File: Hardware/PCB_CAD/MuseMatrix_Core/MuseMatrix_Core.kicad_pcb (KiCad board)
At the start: 2 copper layers, 65 parts, among them J10 Conn_01x03_Pin, J11 Conn_01x03_Pin, J12 Conn_01x03_Pin, J2 Conn_01x07_Socket, J3 Conn_01x03_Pin, J4 Conn_01x07_Socket, J5 Conn_01x07_Socket, J6 Conn_01x03_Pin, J7 Conn_01x03_Pin, J8 Conn_01x03_Pin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

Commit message: more pcb edit
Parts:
- added H1: MountingHole, MountingHole:MountingHole_2.1mm, F.Cu at (25.0, 17.5)
- added H2: MountingHole, MountingHole:MountingHole_2.1mm, F.Cu at (50.0, 17.5)
- added H3: MountingHole, MountingHole:MountingHole_2.1mm, F.Cu at (50.0, 173.5)
- added H4: MountingHole, MountingHole:MountingHole_2.1mm, F.Cu at (25.0, 173.5)
- added H5: MountingHole, MountingHole:MountingHole_2.1mm, F.Cu at (56.0, 17.5)
- added H6: MountingHole, MountingHole:MountingHole_2.1mm, F.Cu at (81.0, 17.5)
- added H7: MountingHole, MountingHole:MountingHole_2.1mm, F.Cu at (56.0, 128.0)
- added H8: MountingHole, MountingHole:MountingHole_2.1mm, F.Cu at (81.0, 128.0)
- added J1: Raspberry_Pi_4, Connector_PinHeader_1.00mm:PinHeader_2x16_P1.00mm_Vertical, F.Cu at (114.0, 56.5)
- added J13: Conn_01x10_Socket, Library:Skedd connector x10, F.Cu at (24.5, 79.0)
- added J14: Jack-DC, Connector_Audio:Jack_3.5mm_CUI_SJ-3523-SMT_Horizontal, F.Cu at (113.4, 21.7)
- added J17: Conn_01x06_Pin, Library:Skedd connector x6, F.Cu at (31.3, 171.0)
- added J18: Conn_01x06_Pin, Library:Skedd connector x6, F.Cu at (58.5, 29.1)
- added R29: 330, Resistor_SMD:R_0402_1005Metric, F.Cu at (142.0, 52.0)
- added R30: 330, Resistor_SMD:R_0402_1005Metric, F.Cu at (142.0, 54.0)
- added R31: 330, Resistor_SMD:R_0402_1005Metric, F.Cu at (142.0, 56.0)
- added U4: 6N138, Package_DIP:DIP-8_W7.62mm_LongPads, F.Cu at (128.7, 74.2)
- J2: value Conn_01x07_Socket -> Conn_01x03_Pin; footprint Connector_JST:JST_EH_B7B-EH-A_1x07_P2.50mm_Vertical -> Connector_JST:JST_EH_B3B-EH-A_1x03_P2.50mm_Vertical; moved to B.Cu
- J3: value Conn_01x03_Pin -> Conn_01x10_Socket; footprint Connector_JST:JST_EH_B3B-EH-A_1x03_P2.50mm_Vertical -> Library:Skedd connector x10
- J4: value Conn_01x07_Socket -> DIN-5; footprint Connector_JST:JST_EH_B7B-EH-A_1x07_P2.50mm_Vertical -> Connector_JST:JST_EH_B5B-EH-A_1x05_P2.50mm_Vertical
- R1: value LDR07 -> 330; footprint OptoDevice:R_LDR_5.1x4.3mm_P3.4mm_Vertical -> Capacitor_SMD:C_0402_1005Metric
- R11, R12, R20, R21, R22, R6: footprint OptoDevice:R_LDR_5.1x4.3mm_P3.4mm_Vertical -> Library:LDR 2.5 horizontal
- R2: value 330 -> LDR07; footprint Capacitor_SMD:C_0402_1005Metric -> Library:LDR 2.5 horizontal
- R28: footprint Potentiometer_THT:Potentiometer_Bourns_PTV09A-1_Single_Vertical -> Resistor_SMD:R_0402_1005Metric
- moved RV1 158.9 mm to (97.0, 168.3), turned to 90 degrees
- moved RV7 156.9 mm to (97.0, 122.0), turned to 90 degrees
- moved RV3 155.2 mm to (97.0, 152.9), turned to 90 degrees
- moved RV5 154.5 mm to (97.0, 137.4), turned to 90 degrees
- moved RV2 139.2 mm to (111.3, 168.3), turned to 90 degrees
- moved RV8 137.0 mm to (111.3, 122.0), turned to 90 degrees
- moved RV4 135.0 mm to (111.3, 152.9), turned to 90 degrees
- moved RV6 134.2 mm to (111.3, 137.4), turned to 90 degrees
- moved R17 132.9 mm to (65.0, 18.0)
- moved Q8 113.7 mm to (36.0, 28.0), turned to 180 degrees
- moved R26 108.4 mm to (81.5, 47.5)
- moved U1 105.8 mm to (101.6, 104.0), turned to 90 degrees
- moved D5 104.0 mm to (70.5, 18.0)
- moved Q4 102.5 mm to (45.0, 174.0), turned to 90 degrees
- moved R18 100.1 mm to (65.0, 53.0)
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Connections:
- D1 pad 2: (no net) -> Net-(D1-A)
- J2 pad 1: /Column_7_Rows/d1 -> GND
- J2 pad 2: /Column_7_Rows/d2 -> /Column_7_Rows/Column_voltage
- J2 pad 3: /Column_7_Rows/d3 -> +3.3V
- J3 pad 1: GND -> /Column_7_Rows/d1
- J3 pad 2: /Column_7_Rows/Column_voltage -> /Column_7_Rows/d2
- J3 pad 3: +3.3V -> /Column_7_Rows/d3
- J4 pad 1: /Column_7_Rows/d1 -> unconnected-(J4-Pad1)
- J4 pad 2: /Column_7_Rows/d2 -> unconnected-(J4-Pad2)
- J4 pad 3: /Column_7_Rows/d3 -> (no net)
- J4 pad 4: /Column_7_Rows/d4 -> (no net)
- J4 pad 5: /Column_7_Rows/d5 -> (no net)
- J5 pad 1: /Main_board/jst0 -> unconnected-(J5-Pin_1-Pad1)
- Q1 pad 2: unconnected-(R3-Pad1) -> Net-(Q1-B)
- Q5 pad 3: /Column_7_Rows/d5 -> /Column_7_Rows/d5_0
- Q6 pad 3: /Column_7_Rows/d6 -> /Column_7_Rows/d6_0
- Q7 pad 3: /Column_7_Rows/d7 -> /Column_7_Rows/d7_0
- R1 pad 1: unconnected-(R3-Pad1) -> /Column_7_Rows/column_voltage
- R1 pad 2: +3.3V -> Net-(D1-A)
- R17 pad 1: /Column_7_Rows/column_voltage -> /Column_7_Rows/column_voltage2
- R18 pad 1: /Column_7_Rows/column_voltage -> /Column_7_Rows/column_voltage2
- R19 pad 1: /Column_7_Rows/column_voltage -> /Column_7_Rows/column_voltage2
- R2 pad 1: /Column_7_Rows/column_voltage -> Net-(Q1-B)
- R2 pad 2: (no net) -> +3.3V
- R26 pad 2: /Column_7_Rows/d5 -> /Column_7_Rows/d5_0
- R27 pad 2: /Column_7_Rows/d6 -> /Column_7_Rows/d6_0
- R28 pad 2: /Column_7_Rows/d7 -> /Column_7_Rows/d7_0
- R3 pad 1: unconnected-(R3-Pad1) -> Net-(Q1-B)
- U1 pad 10: unconnected-(U1-~{CS}/SHDN-Pad10) -> /Octaves board/select
- U1 pad 13: unconnected-(U1-CLK-Pad13) -> /Octaves board/ADC_clock
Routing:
- net /Column_7_Rows/column_voltage: track 0.00 -> 143.9 mm, vias 0 -> 2
- net /Column_7_Rows/d6_1: track 0.00 -> 119.7 mm, vias 0 -> 2
- net /Column_7_Rows/d7_0: track 0.00 -> 118.0 mm
- net /Column_7_Rows/d4: track 0.00 -> 116.4 mm
- net /Column_7_Rows/d7_1: track 0.00 -> 115.3 mm, vias 0 -> 2
- net /Column_7_Rows/d5_1: track 0.00 -> 112.5 mm
- net /Column_7_Rows/d3: track 0.00 -> 87.8 mm, vias 0 -> 1
- net /Column_7_Rows/column_voltage2: track 0.00 -> 75.2 mm, vias 0 -> 2
- net /Column_7_Rows/d6_0: track 0.00 -> 71.2 mm
- net Net-(U1-CH1): track 0.00 -> 67.2 mm, vias 0 -> 1
- net Net-(U1-CH3): track 0.00 -> 64.8 mm
- net Net-(U1-CH0): track 0.00 -> 64.2 mm, vias 0 -> 1
- net Net-(U1-CH2): track 0.00 -> 55.6 mm
- net /Column_7_Rows/d2: track 0.00 -> 52.5 mm, vias 0 -> 1
- net /Column_7_Rows/d5_0: track 0.00 -> 43.3 mm, vias 0 -> 1
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- added copper zone on B.Cu, net (none)
- added copper zone on F.Cu, net (none)
- added copper zone on In1.Cu, net +3.3V
- added copper zone on In2.Cu, net GND
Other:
- board outline added: 97 x 161.5 mm
- copper layers 2 -> 4

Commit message: finished pcb + gerbers
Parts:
- added mouse-bite-1mm-slot: VAL**, Library:mouse-bite-1mm-slot, F.Cu at (84.0, 102.0)
- added mouse-bite-1mm-slot: VAL**, Library:mouse-bite-1mm-slot, F.Cu at (84.0, 69.5)
- added mouse-bite-1mm-slot: VAL**, Library:mouse-bite-1mm-slot, F.Cu at (53.0, 40.0)
- added mouse-bite-1mm-slot: VAL**, Library:mouse-bite-1mm-slot, F.Cu at (53.0, 113.2)
- J4: footprint Connector_JST:JST_EH_B5B-EH-A_1x05_P2.50mm_Vertical -> Connector_PinHeader_2.54mm:PinHeader_1x05_P2.54mm_Vertical
- J5: value Conn_01x07_Socket -> Conn_01x10_Socket; footprint Connector_JST:JST_EH_B7B-EH-A_1x07_P2.50mm_Vertical -> Library:Skedd connector x10
- moved J4 66.8 mm to (106.1, 30.0), turned to 90 degrees
- moved R31 37.7 mm to (111.8, 33.5), turned to -90 degrees
- moved R30 37.5 mm to (109.5, 35.2)
- moved U4 34.8 mm to (109.2, 45.3), turned to 90 degrees
- moved R29 33.3 mm to (108.8, 50.8), turned to 90 degrees
- moved J1 10.9 mm to (103.5, 53.8)
- moved U3 5.75 mm to (101.8, 83.5)
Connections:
- J1 pad 1: /Main_board/3.3 -> +3.3V
- J1 pad 17: /Main_board/3.3 -> +3.3V
- J4 pad 3: (no net) -> unconnected-(J4-Pad3)
- J4 pad 4: (no net) -> Net-(J4-Pad4)
- J4 pad 5: (no net) -> Net-(U4-VO2)
- J5 pad 1: unconnected-(J5-Pin_1-Pad1) -> /Main_board/jst0
- U2 pad 16: /Main_board/3.3 -> +3.3V
- U3 pad 16: /Main_board/3.3 -> +3.3V
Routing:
- net /Octaves board/DATA_IN_ADC: track 0.00 -> 56.2 mm, vias 0 -> 1
- net /Main_board/LOAD_165: track 0.00 -> 51.6 mm, vias 0 -> 1
- net /Octaves board/DATA_OUT_ADC: track 0.00 -> 50.5 mm, vias 0 -> 1
- net /Octaves board/select: track 0.00 -> 48.0 mm
- net /Octaves board/ADC_clock: track 0.00 -> 46.9 mm
- net /Main_board/clock_165: track 0.00 -> 45.5 mm, vias 0 -> 1
- net /Main_board/LATCH_595: track 0.00 -> 29.1 mm, vias 0 -> 1
- net /Main_board/DATA_OUT_165: track 0.00 -> 23.0 mm, vias 0 -> 2
- net /Main_board/c6: track 0.00 -> 23.0 mm
- net /Main_board/DATA_IN_595: track 0.00 -> 23.0 mm
- net /Main_board/clock_595: track 0.00 -> 20.3 mm, vias 0 -> 1
- net /Main_board/c5: track 0.00 -> 18.5 mm
- net /Main_board/jst0: track 0.00 -> 17.1 mm
- net /Main_board/c0: track 0.00 -> 16.4 mm
- net /Main_board/jst6: track 0.00 -> 16.0 mm, vias 0 -> 1
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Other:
- outline, holes or cut-outs redrawn

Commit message: update
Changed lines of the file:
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@@
 			(outputformat 1)
 			(mirror no)
-			(drillshape 1)
+			(drillshape 0)
 			(scaleselection 1)
-			(outputdirectory "")
+			(outputdirectory "gerbers/")
 		)
 	)
@@
 			(layers "*.Cu" "*.Mask")
 			(remove_unused_layers no)
-			(roundrect_rratio 0.147059)
+			(roundrect_rratio 0.1470588235)
 			(net 1 "GND")
 			(pinfunction "Pin_1")
@@
 			(layers "*.Cu" "*.Mask")
 			(remove_unused_layers no)
-			(roundrect_rratio 0.147059)
+			(roundrect_rratio 0.1470588235)
 			(net 1 "GND")
 			(pinfunction "Pin_1")
@@
 			(layers "*.Cu" "*.Mask")
 			(remove_unused_layers no)
-			(roundrect_rratio 0.147059)
+			(roundrect_rratio 0.1470588235)
 			(net 1 "GND")
 			(pinfunction "Pin_1")
@@
 			(layers "*.Cu" "*.Mask")
 			(remove_unused_layers no)
-			(roundrect_rratio 0.147059)
+			(roundrect_rratio 0.1470588235)
 			(net 1 "GND")
 			(pinfunction "Pin_1")
@@
 			(layers "*.Cu" "*.Mask")
 			(remove_unused_layers no)
-			(roundrect_rratio 0.147059)
+			(roundrect_rratio 0.1470588235)
 			(net 1 "GND")
 			(pinfunction "Pin_1")
@@
 			(layers "*.Cu" "*.Mask")
 			(remove_unused_layers no)
-			(roundrect_rratio 0.147059)
+			(roundrect_rratio 0.1470588235)
 			(net 1 "GND")
 			(pinfunction "Pin_1")
@@
 			(layers "*.Cu" "*.Mask")
 			(remove_unused_layers no)
-			(roundrect_rratio 0.147059)
+			(roundrect_rratio 0.1470588235)
 			(net 1 "GND")
 			(pinfunction "Pin_1")
@@
 			(layers "*.Cu" "*.Mask")
 			(remove_unused_layers no)
-			(roundrect_rratio 0.147059)
+			(roundrect_rratio 0.1470588235)
 			(net 1 "GND")
 			(pinfunction "Pin_1")

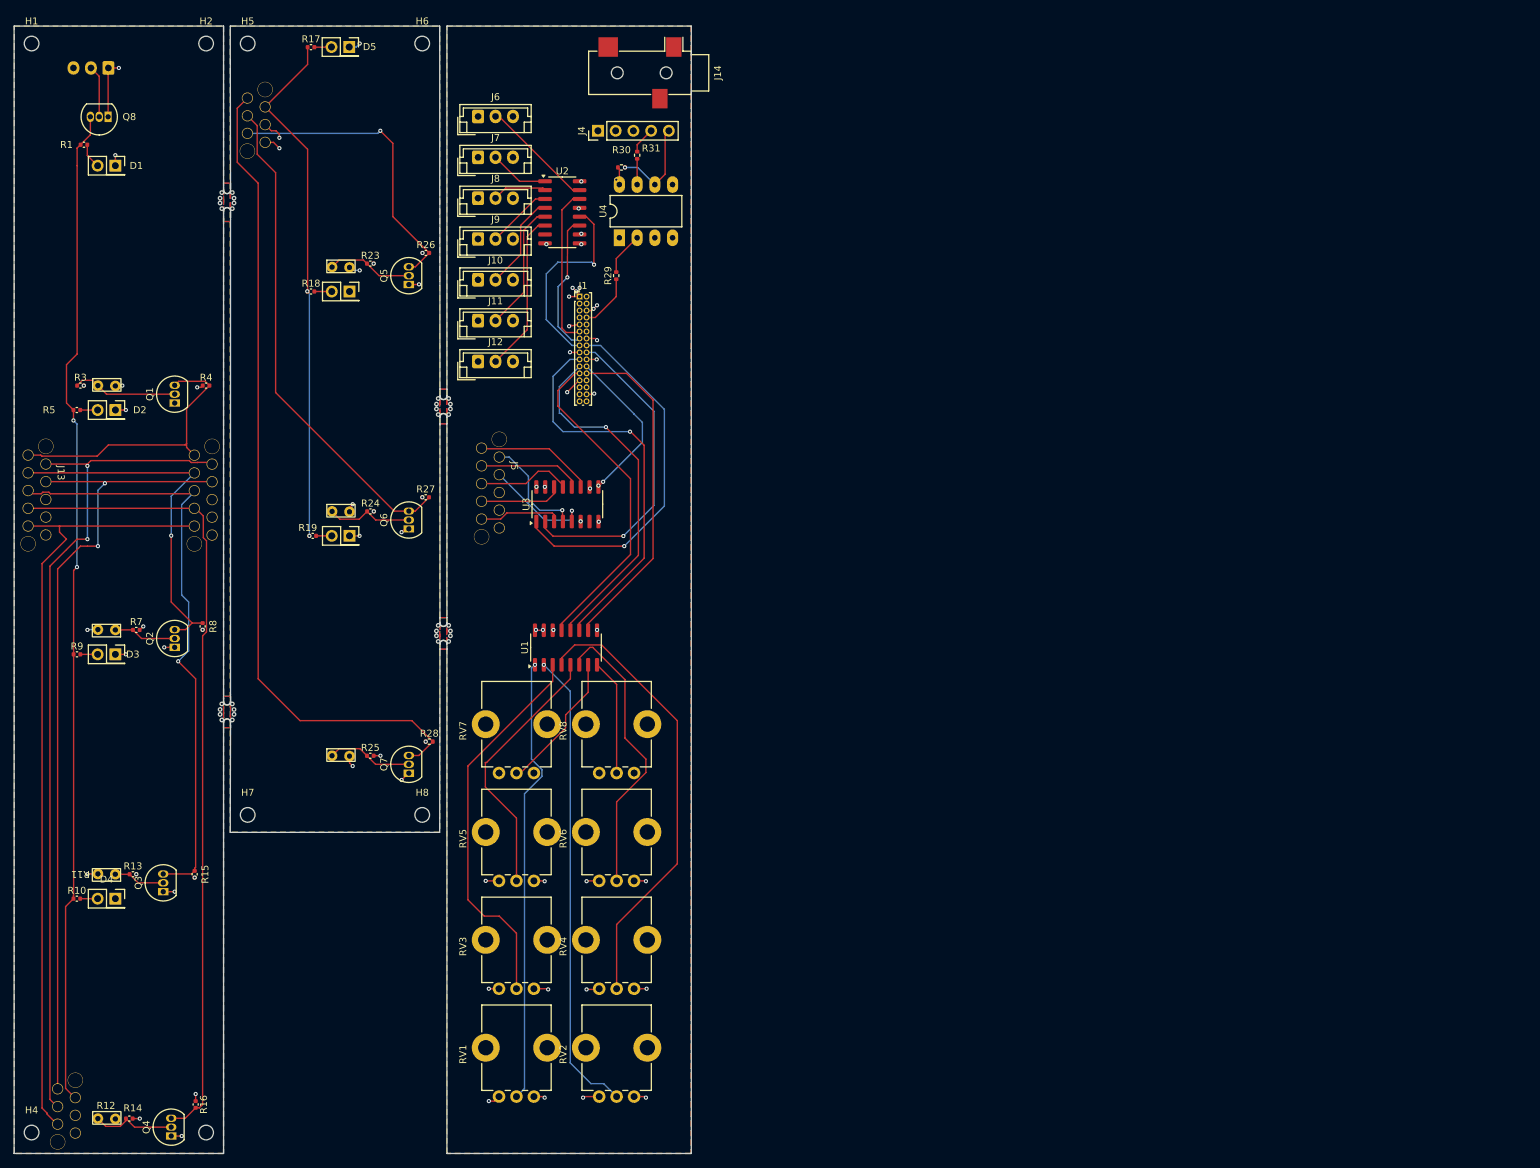
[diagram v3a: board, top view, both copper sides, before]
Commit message: separated in 2 boards
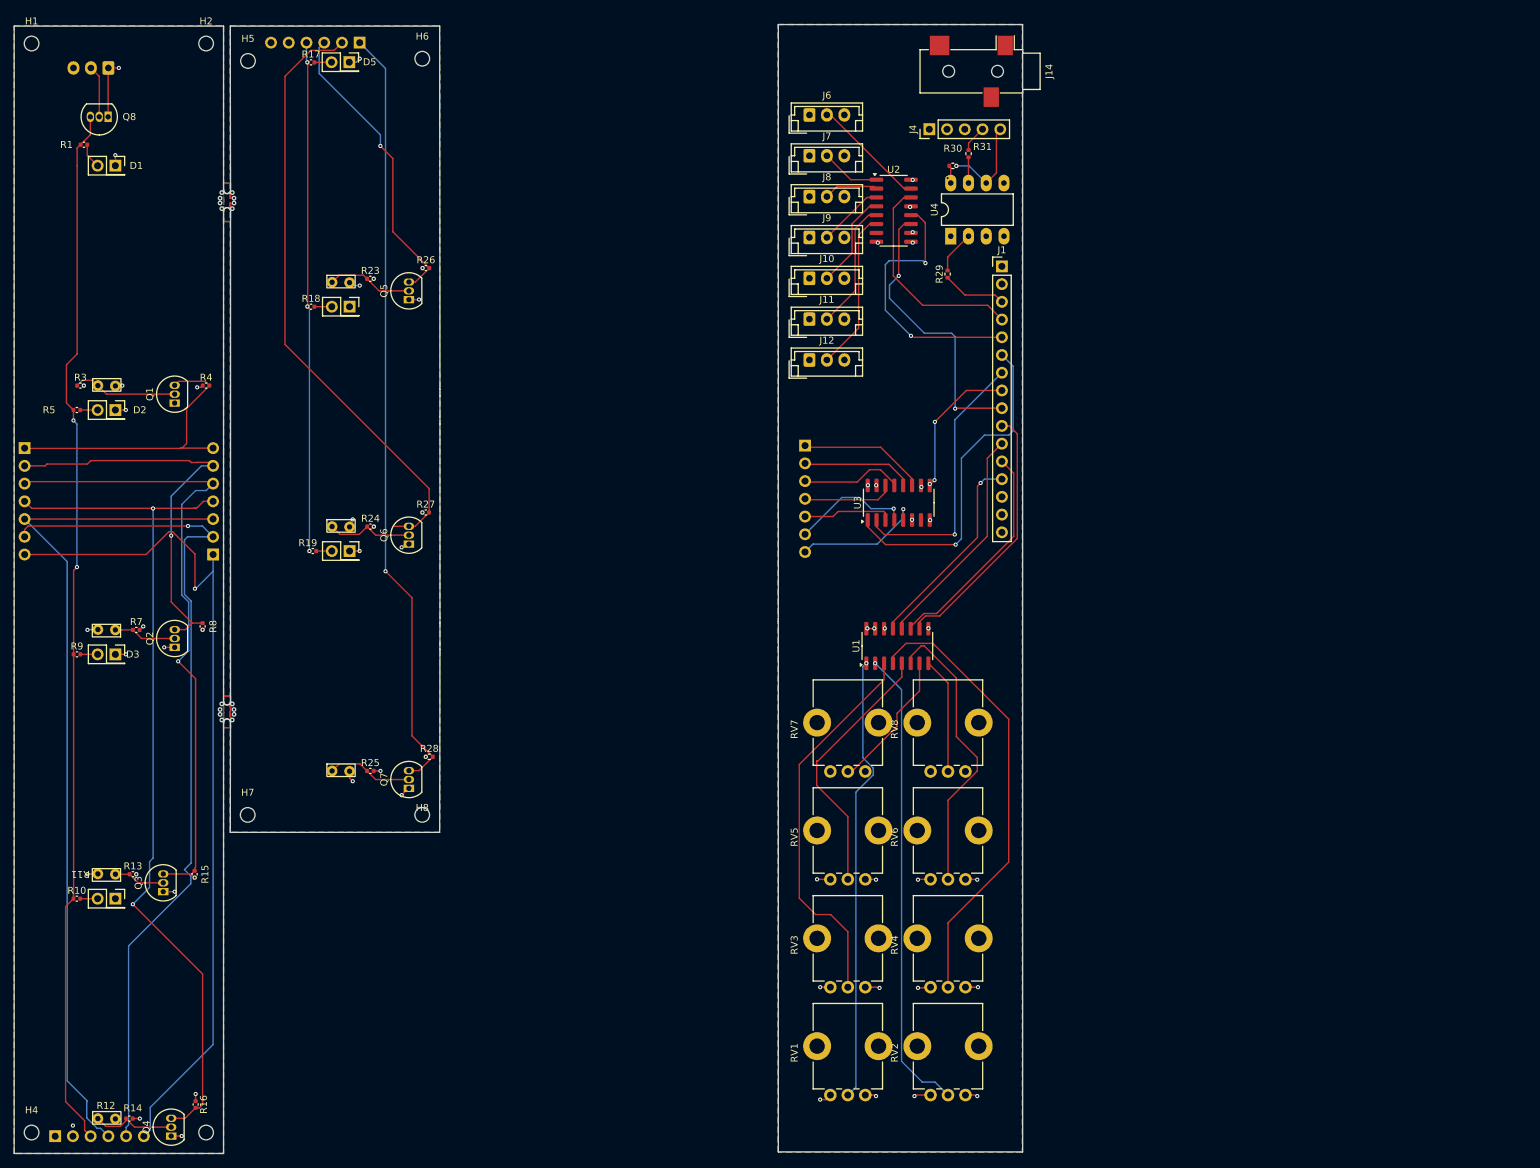
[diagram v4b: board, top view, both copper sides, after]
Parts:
- removed the mouse-bite-1mm-slot at (84.0, 102.0)
- removed the mouse-bite-1mm-slot at (84.0, 69.5)
- J1: footprint Connector_PinHeader_1.00mm:PinHeader_2x16_P1.00mm_Vertical -> Connector_PinHeader_2.54mm:PinHeader_1x16_P2.54mm_Vertical
- J13, J5: value Conn_01x10_Socket -> Conn_01x07_Socket; footprint Library:Skedd connector x10 -> Connector_PinHeader_2.54mm:PinHeader_1x07_P2.54mm_Horizontal; moved to B.Cu
- J17, J18: footprint Library:Skedd connector x6 -> Connector_PinHeader_2.54mm:PinHeader_1x06_P2.54mm_Horizontal; moved to B.Cu
- J3: footprint Library:Skedd connector x10 -> Connector_PinHeader_2.54mm:PinHeader_1x07_P2.54mm_Horizontal; moved to B.Cu
- moved J1 60.7 mm to (164.0, 49.4)
- moved J10 47.5 mm to (136.4, 51.1)
- moved J11 47.5 mm to (136.4, 57.0)
- moved J12 47.5 mm to (136.4, 62.8)
- moved J14 47.5 mm to (160.9, 21.5)
- moved J4 47.5 mm to (153.6, 29.8)
- moved J6 47.5 mm to (136.4, 27.7)
- moved J7 47.5 mm to (136.4, 33.6)
- moved J8 47.5 mm to (136.4, 39.4)
- moved J9 47.5 mm to (136.4, 45.3)
- moved R29 47.5 mm to (156.2, 50.5)
- moved R30 47.5 mm to (157.0, 35.0)
- moved R31 47.5 mm to (159.2, 33.3)
- moved RV1 47.5 mm to (144.4, 168.1)
- moved RV3 47.5 mm to (144.4, 152.7)
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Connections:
- J1 pad 32: unconnected-(J1-GPIO12/PWM0-Pad32) -> (no net)
- J18 pad 1: GND -> /Column_7_Rows/d7_0
- J18 pad 2: +3.3V -> /Column_7_Rows/d6_0
- J18 pad 3: /Column_7_Rows/column_voltage2 -> /Column_7_Rows/d5_0
- J18 pad 4: /Column_7_Rows/d5_0 -> /Column_7_Rows/column_voltage2
- J18 pad 5: /Column_7_Rows/d6_0 -> +3.3V
- J18 pad 6: /Column_7_Rows/d7_0 -> GND
- J3 pad 1: /Column_7_Rows/d1 -> /Column_7_Rows/d7_1
- J3 pad 2: /Column_7_Rows/d2 -> /Column_7_Rows/d6_1
- J3 pad 3: /Column_7_Rows/d3 -> /Column_7_Rows/d5_1
- J3 pad 5: /Column_7_Rows/d5_1 -> /Column_7_Rows/d3
- J3 pad 6: /Column_7_Rows/d6_1 -> /Column_7_Rows/d2
- J3 pad 7: /Column_7_Rows/d7_1 -> /Column_7_Rows/d1
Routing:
- net /Octaves board/DATA_IN_ADC: track 56.2 -> 31.9 mm, vias 1 -> 0
- net /Main_board/clock_595: track 20.3 -> 41.2 mm, vias 1 -> 2
- net /Octaves board/DATA_OUT_ADC: track 50.5 -> 32.5 mm, vias 1 -> 0
- net /Octaves board/ADC_clock: track 46.9 -> 29.4 mm, vias 0 -> 1
- net /Column_7_Rows/d6_0: track 71.2 -> 87.0 mm
- net /Main_board/LATCH_595: track 29.1 -> 39.5 mm, vias 1 -> 2
- net /Octaves board/select: track 48.0 -> 37.6 mm
- net /Raspberry_connections/GND: track 10.7 -> 2.00 mm, vias 7 -> 0
- net /Column_7_Rows/d4: track 115.6 -> 124.1 mm, vias 0 -> 2
- net /Column_7_Rows/d5_1: track 112.5 -> 120.7 mm
- net /Main_board/DATA_IN_595: track 23.0 -> 31.0 mm
- net /Column_7_Rows/d7_1: track 115.3 -> 123.1 mm, vias 2 -> 1
- net +3.3V: track 37.6 -> 30.0 mm, vias 32 -> 27
- net /Column_7_Rows/d7_0: track 118.0 -> 110.9 mm, vias 0 -> 1
- net /Main_board/clock_165: track 45.5 -> 38.7 mm
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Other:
- board size 97 x 161.5 mm -> 144.5 x 161.7 mm
